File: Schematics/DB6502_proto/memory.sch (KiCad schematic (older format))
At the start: 6 parts, among them U19 62256, U20 62256, U21 28C256

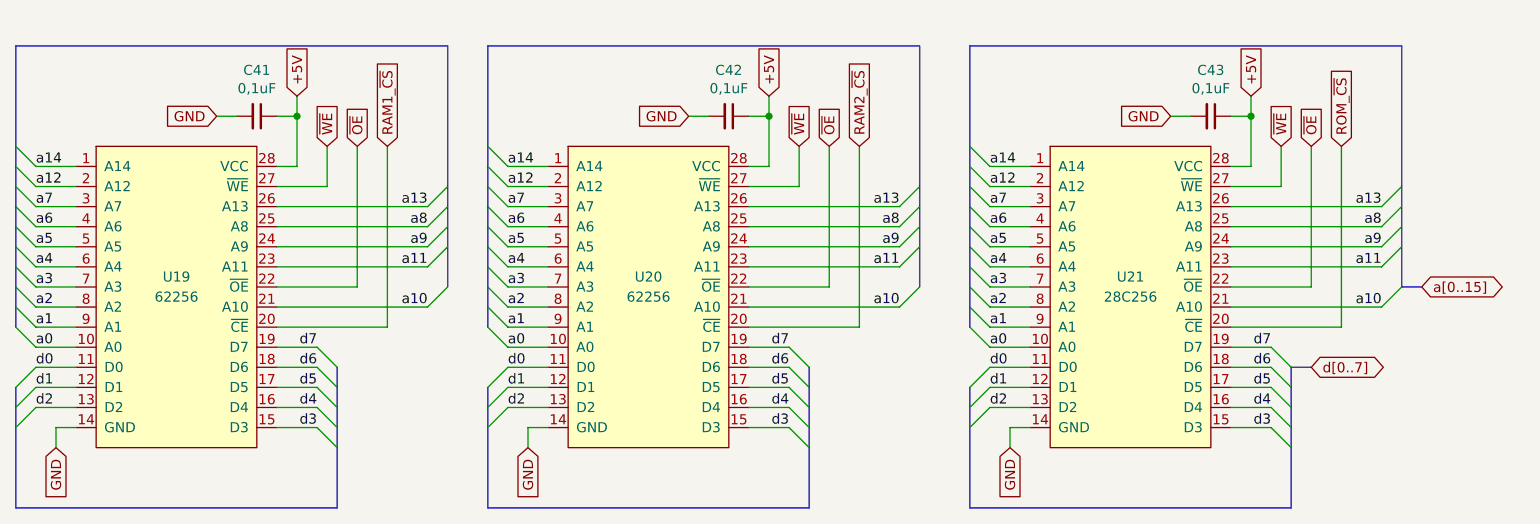
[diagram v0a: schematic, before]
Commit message: Replaced nWE with nWR and nOE with nRD
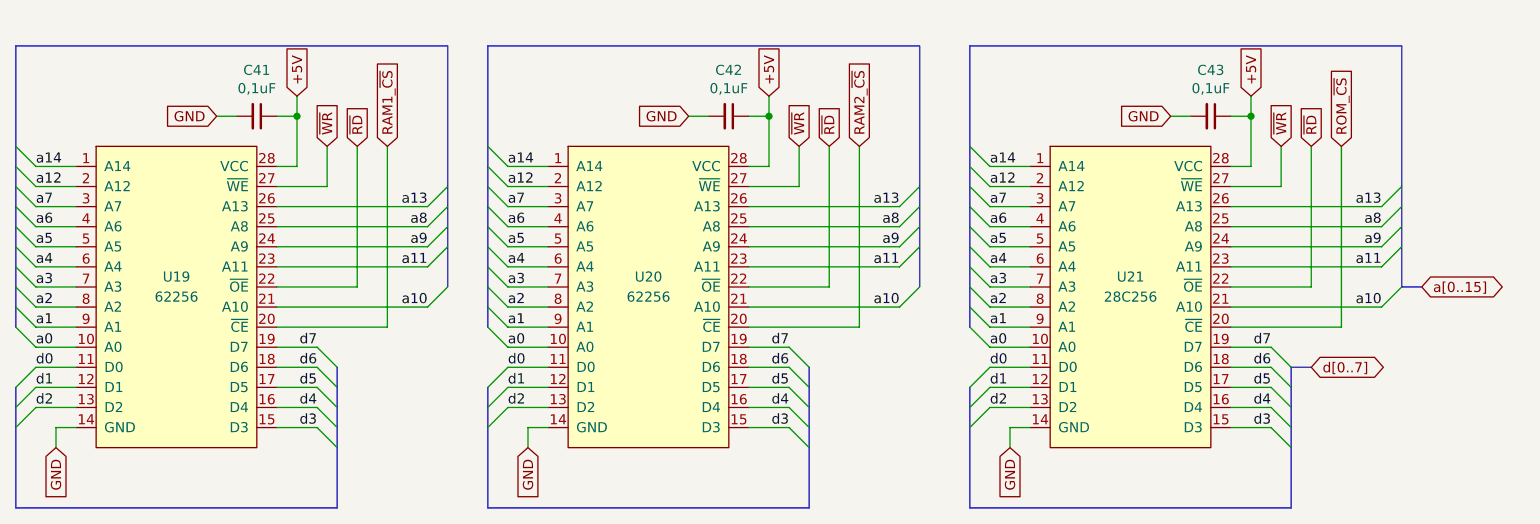
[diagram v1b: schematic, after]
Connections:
- net ~OE renamed ~RD
- net ~WE renamed ~WR
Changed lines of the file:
@@
 	2300 1450 2200 1450
 Text GLabel 2450 1350 1    50   Input ~ 0
-~WE
+~WR
 Wire Wire Line
 	2450 1350 2450 1550
@@
 	2450 1550 2200 1550
 Text GLabel 2600 1350 1    50   Input ~ 0
-~OE
+~RD
 Text GLabel 2750 1350 1    50   Input ~ 0
 RAM1_~CS
@@
 	4650 1450 4550 1450
 Text GLabel 4800 1350 1    50   Input ~ 0
-~WE
+~WR
 Wire Wire Line
 	4800 1350 4800 1550
@@
 	4800 1550 4550 1550
 Text GLabel 4950 1350 1    50   Input ~ 0
-~OE
+~RD
 Text GLabel 5100 1350 1    50   Input ~ 0
 RAM2_~CS
@@
 	7050 1450 6950 1450
 Text GLabel 7200 1350 1    50   Input ~ 0
-~WE
+~WR
 Wire Wire Line
 	7200 1350 7200 1550
@@
 	7200 1550 6950 1550
 Text GLabel 7350 1350 1    50   Input ~ 0
-~OE
+~RD
 Text GLabel 7500 1350 1    50   Input ~ 0
 ROM_~CS

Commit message: Updated schematic to reflect new wait state generator design
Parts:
- removed C41, C42, C43: 0,1uF, Capacitor_THT:C_Disc_D5.0mm_W2.5mm_P2.50mm, symbol Device:C_Small
- removed U19, U20: 62256, Package_DIP:DIP-28_W15.24mm_Socket, symbol 6502:62256
- removed U21: 28C256, Package_DIP:DIP-28_W15.24mm_Socket, symbol 6502:28C256
